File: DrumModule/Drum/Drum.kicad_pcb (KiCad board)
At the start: 2 copper layers, 39.4 x 99.1 mm, 44 parts, among them J1 Barrel_Jack_Switch, J2 Barrel_Jack_Switch, J3 Conn_02x05_Odd_Even, Q1 MMBT3904, U1 74HC74, U2 MIC5205-5.0YM5, U3 LM2904DR, U4 LM2904DR, U5 LM2904DR

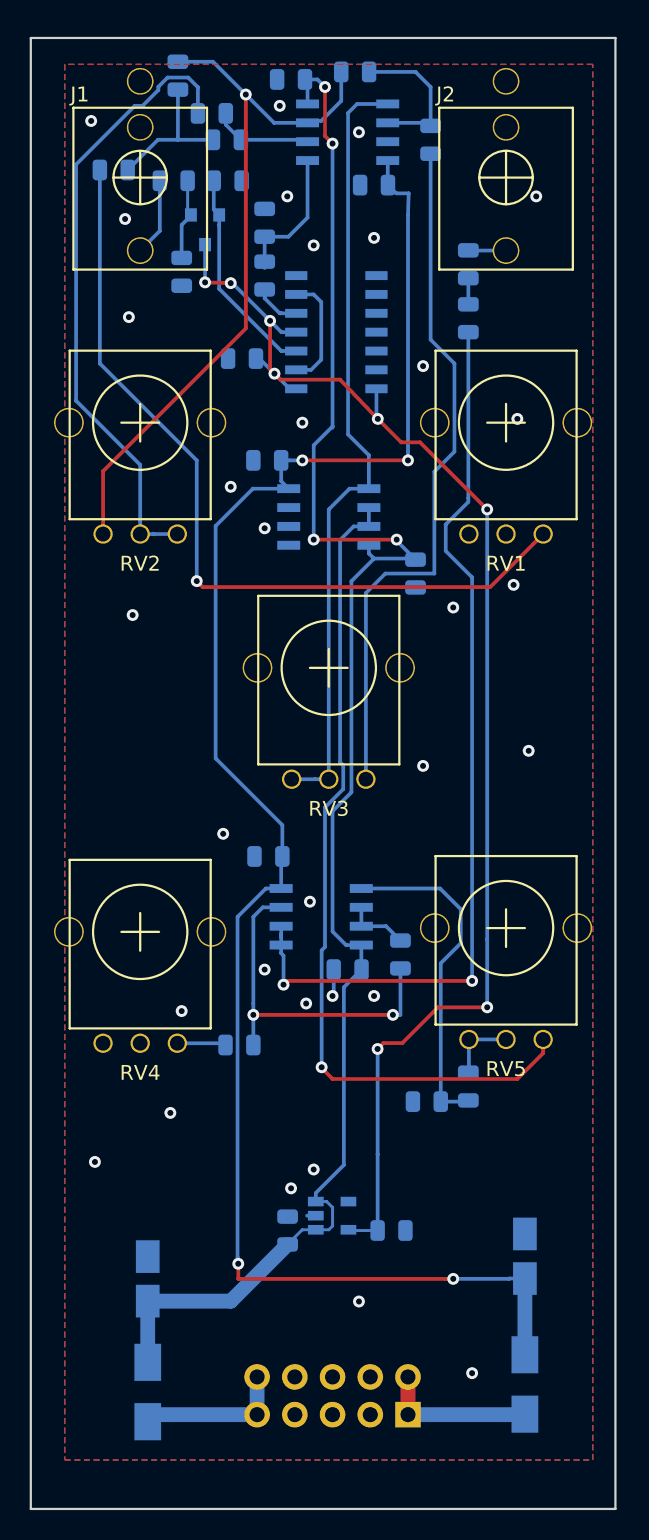
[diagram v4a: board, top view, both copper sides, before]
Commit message: IO faceplate added for the drum
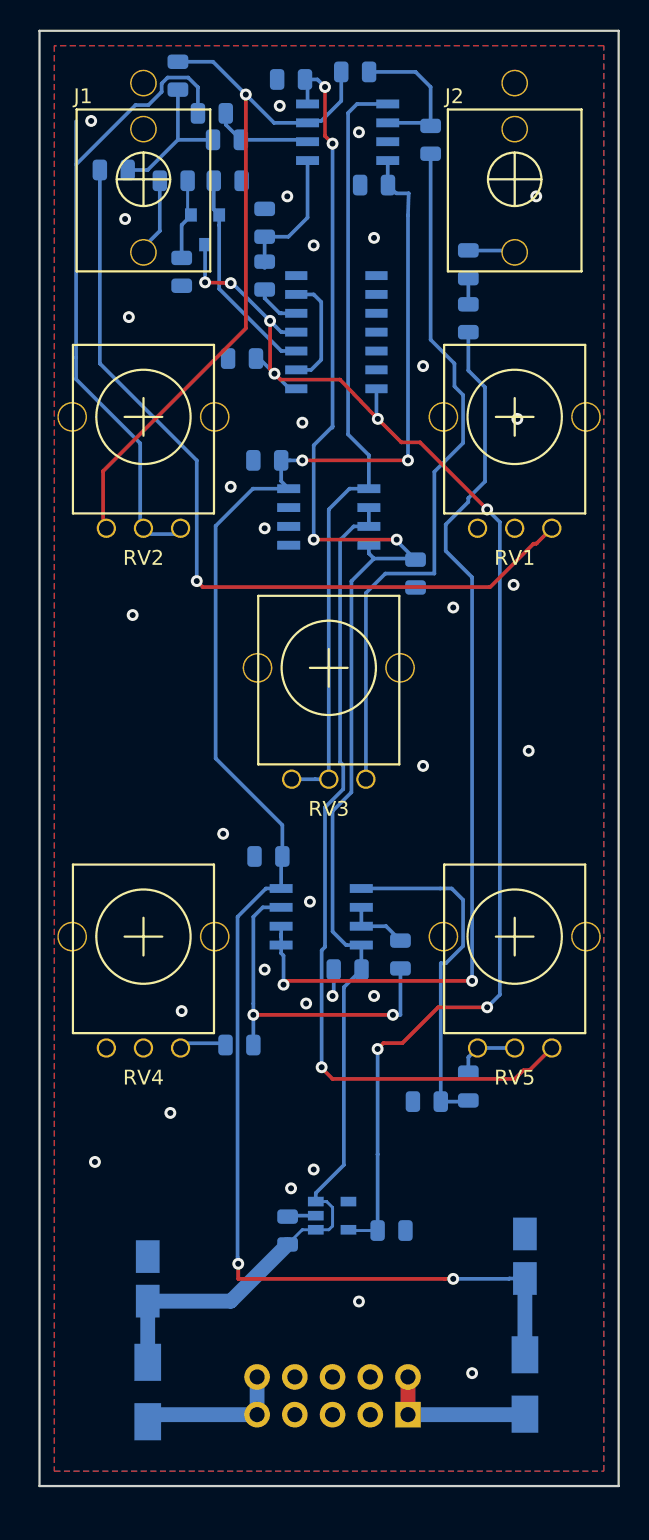
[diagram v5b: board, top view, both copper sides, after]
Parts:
- moved RV5 0.82 mm to (170.0, 107.0)
- moved RV1 0.70 mm to (170.0, 72.0)
- moved J2 0.59 mm to (170.0, 56.0)
- moved RV2 0.45 mm to (145.0, 72.0)
- moved RV4 0.39 mm to (145.0, 107.0)
- moved J1 0.25 mm to (145.0, 56.0)
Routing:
- net Net-(R6-Pad2): track 42.0 -> 45.1 mm
- net GND: track 2.40 -> 3.74 mm
- net Net-(R10-Pad1): track 61.9 -> 62.8 mm
- net Net-(C16-Pad1): track 22.7 -> 23.5 mm
- net Net-(R7-Pad1): track 55.4 -> 56.1 mm
- net +5V: track 94.4 -> 95.1 mm
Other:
- board size 39.4 x 99.1 mm -> 39 x 98 mm
